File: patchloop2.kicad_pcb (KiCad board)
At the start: 2 copper layers, 36 x 34 mm, 12 parts, among them J1 8P8C, J2 Conn_Coaxial, J3 8P8C

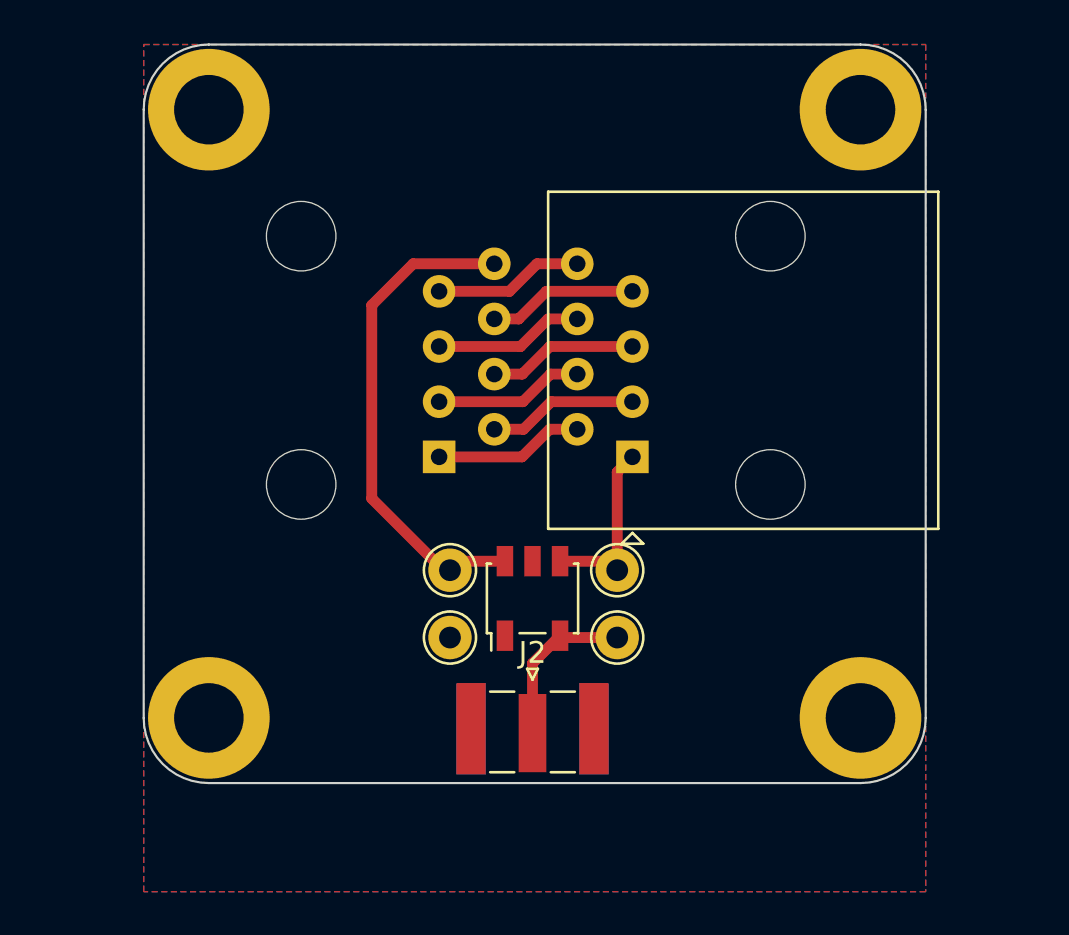
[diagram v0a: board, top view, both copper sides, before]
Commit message: Use well known Parts, move to SMD only
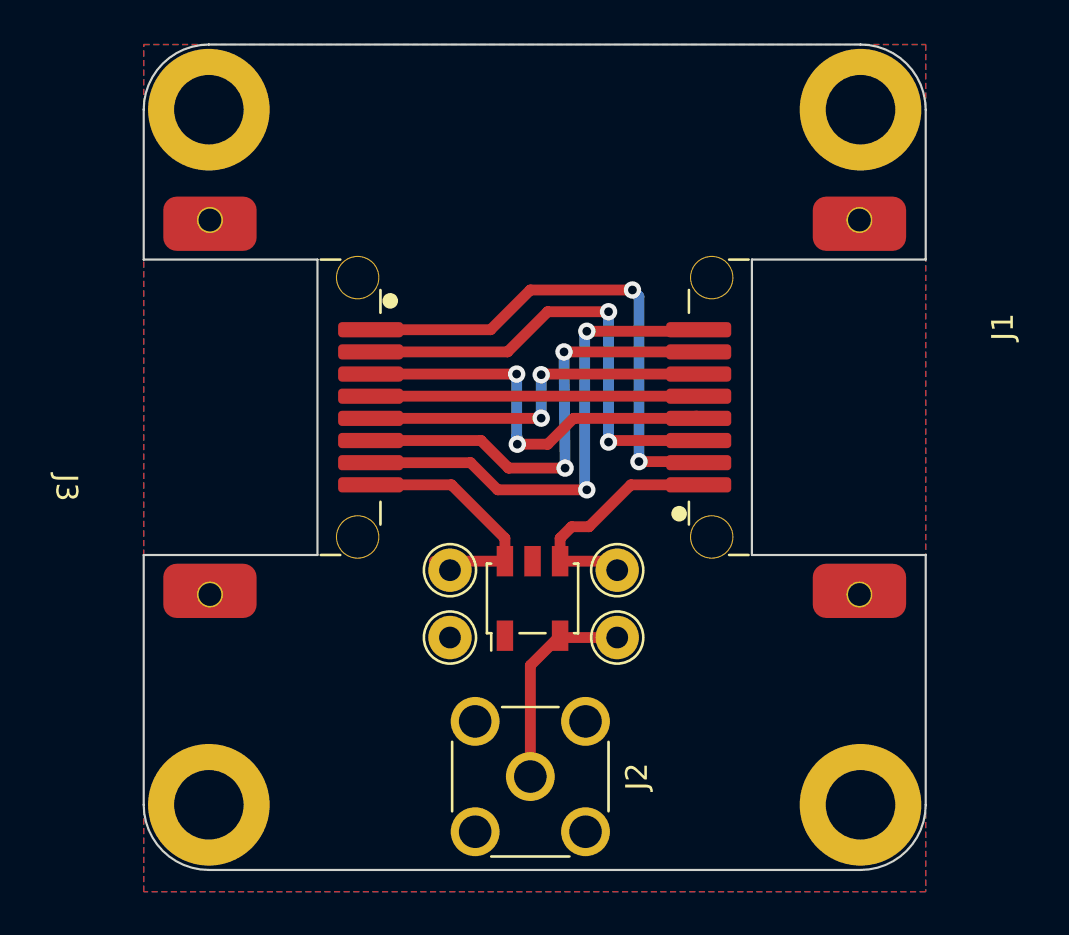
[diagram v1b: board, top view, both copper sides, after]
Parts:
- J1: value 8P8C -> MJ88-B011-JRVS1-P; footprint Connector_RJ:RJ45_Amphenol_54602-x08_Horizontal -> s0_Connector_Heling:MJ88-B011-JRVS1-P
- J2: footprint Connector_Coaxial:SMA_Samtec_SMA-J-P-X-ST-EM1_EdgeMount -> Connector_Coaxial:SMA_Molex_73251-2200_Horizontal
- J3: value 8P8C -> MJ88-B011-JRVS1-P; footprint Connector_RJ:RJ45_Amphenol_54602-x08_Horizontal -> s0_Connector_Heling:MJ88-B011-JRVS1-P; moved to F.Cu
- moved J3 4.39 mm to (109.8, 76.7), turned to -90 degrees
- moved J1 4.30 mm to (126.2, 76.7)
- moved H1 4.00 mm to (133.0, 95.0)
- moved H3 4.00 mm to (103.0, 95.0)
- moved J2 2.20 mm to (117.8, 93.7), turned to 180 degrees
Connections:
- net Net-(J1-Pad1) renamed /B1
- net Net-(J1-Pad2) renamed /I2
- net Net-(J1-Pad3) renamed /I3
- net Net-(J1-Pad4) renamed /I4
- net Net-(J1-Pad5) renamed /I5
- net Net-(J1-Pad6) renamed /I6
- net Net-(J1-Pad7) renamed /I7
- net Net-(J1-Pad8) renamed /I8
- net Net-(J2-Pad1) renamed /U_Out
- net Net-(J3-Pad8) renamed /B2
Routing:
- net /I2: track 6.89 -> 23.6 mm, vias 0 -> 2
- net /I8: track 6.89 -> 23.0 mm, vias 0 -> 2
- net /I3: track 6.89 -> 22.0 mm, vias 0 -> 2
- net /I7: track 6.89 -> 21.0 mm, vias 0 -> 2
- net /I4: track 6.89 -> 19.0 mm, vias 0 -> 2
- net /B2: track 22.7 -> 11.5 mm
- net /I6: track 6.89 -> 17.1 mm, vias 0 -> 2
- net /I5: track 6.89 -> 15.1 mm
- net /B1: track 7.72 -> 11.1 mm
- net /U_Out: track 7.41 -> 9.57 mm
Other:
- board size 36 x 34 mm -> 36 x 38 mm
- board text added: "PatchLoop R2 github.com/SmithChart/patchloop (Fork von DC4HP 2023) CC-BY-SA 3.0"
- board text removed: "PatchLoop v0.1a (c) DC4HP 2023"
